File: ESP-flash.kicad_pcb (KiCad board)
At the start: 2 copper layers, 20.3 x 32.4 mm, 23 parts, among them J101 USB_B_Micro, J102 USB_C_Receptacle_USB2.0, J103 Conn_01x06, Q101 MMDT3904, SW101 SW_SPDT, U101 ESD PROTECTION, U102 TLV75533PDBV, U103 CH340C

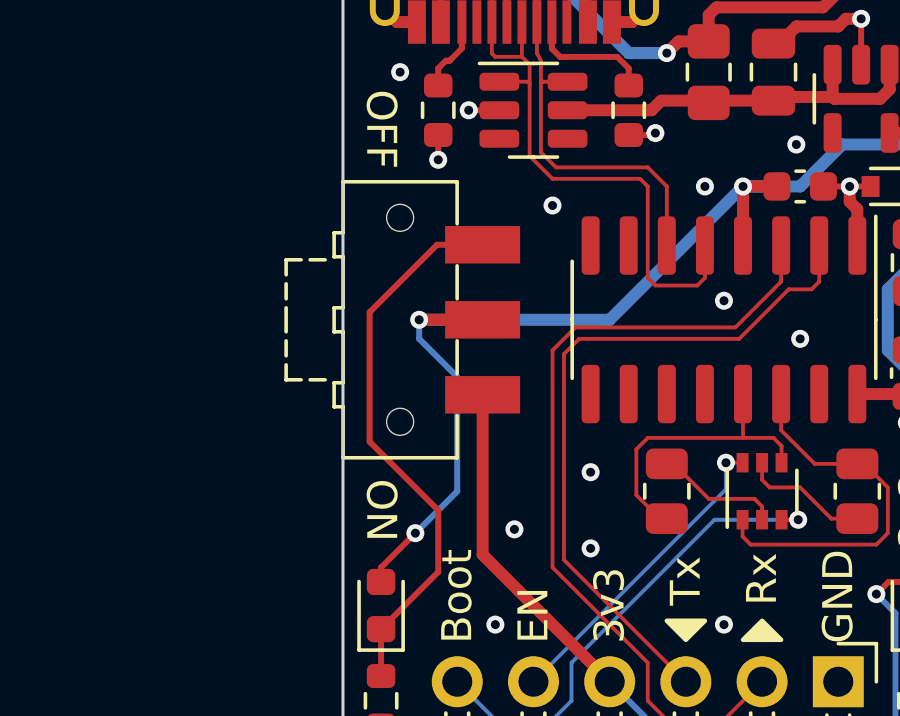
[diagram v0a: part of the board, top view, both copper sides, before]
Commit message: Substitute out-of-stock components
Unsurprising considering how long ago this was last ordered, some of the
components were no longer stocked.
- Green LED (already had a replacement, in other PCB designs)
- Polyfuse (easily found another one on JLCPCB)
- The SPDT switch (couldn't find an exact replacement, and ended up
  using another type with a already-available footprint).
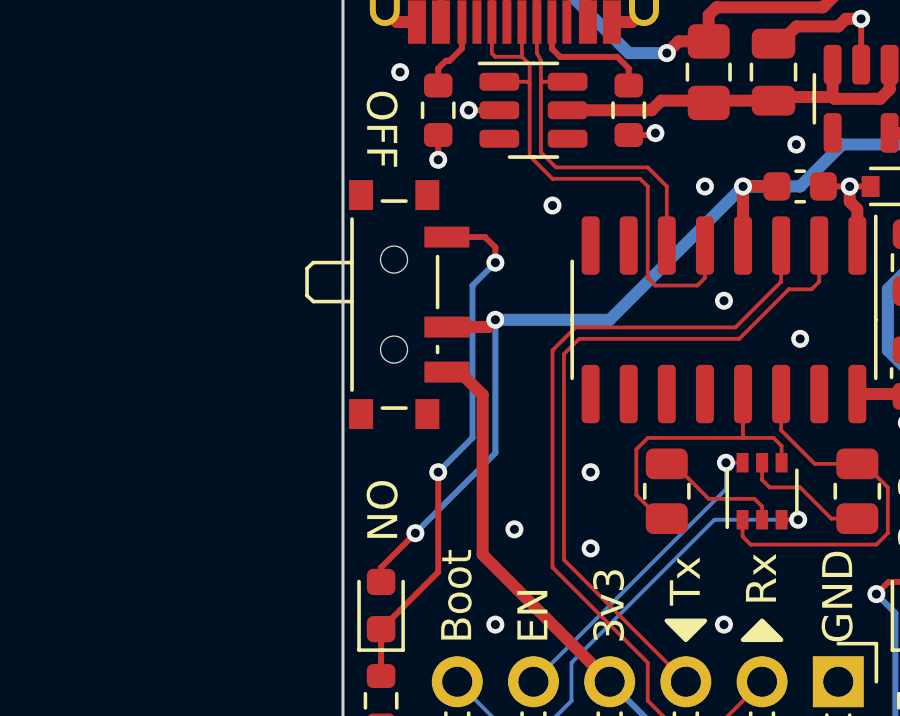
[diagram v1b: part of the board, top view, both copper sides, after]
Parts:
- C103: value 100nF -> C14663
- C104: value 100nF -> 10nF
- SW101: footprint Button_Switch_SMD:SW_SPDT_CK-JS102011SAQN -> Button_Switch_SMD:SW_SPDT_PCM12
- U101: value ESD PROTECTION -> SESRV05-4
- moved SW101 0.52 mm to (134.7, 53.5)
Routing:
- net +3V3: track 51.3 -> 48.4 mm
- net /3v3_{SW}: track 27.8 -> 29.3 mm
- net Net-(D102-K): track 18.6 -> 17.6 mm, vias 0 -> 2
